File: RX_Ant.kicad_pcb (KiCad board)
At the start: 2 copper layers, 100 x 100 mm, 44 parts, among them J1 CONN_COAXIAL, J10 CONN_COAXIAL, J11 CONN_01X06, J12 CONN_01X05, J13 CONN_COAXIAL, J14 CONN_COAXIAL, J15 CONN_COAXIAL, J16 CONN_01X01, J17 CONN_01X01, J18 CONN_01X01, J19 CONN_01X01, J2 CONN_COAXIAL, J20 CONN_01X01, J21 CONN_01X01, J22 CONN_01X01, J23 CONN_01X01, J3 CONN_COAXIAL, J4 CONN_COAXIAL, J5 CONN_COAXIAL, J6 CONN_COAXIAL, J7 CONN_COAXIAL, J8 CONN_COAXIAL, J9 CONN_COAXIAL

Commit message: RTM 1
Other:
- board text added: "+12 In"
- board text added: "+12V_In"
- board text added: "Alex RX In Board"
- board text added: "Alex TX Out Board"
- board text added: "Ant_1"
- board text added: "Ant_2"
- board text added: "Ant_3"
- board text added: "BYPASS"
- board text added: "EXT1"
- board text added: "EXT2"
- board text added: "From HPF Out"
- board text added: "Gnd"
- board text added: "RX2 IN"
- board text added: "RX2_In"
- board text added: "RX3_In"
- board text added: "RX_Bypass_Out"
- board text added: "To HPF In"
- board text added: "To_RX 1"
- board text added: "To_RX 2"
- board text added: "XVTR RX"
- board text added: "Xvtr_In"

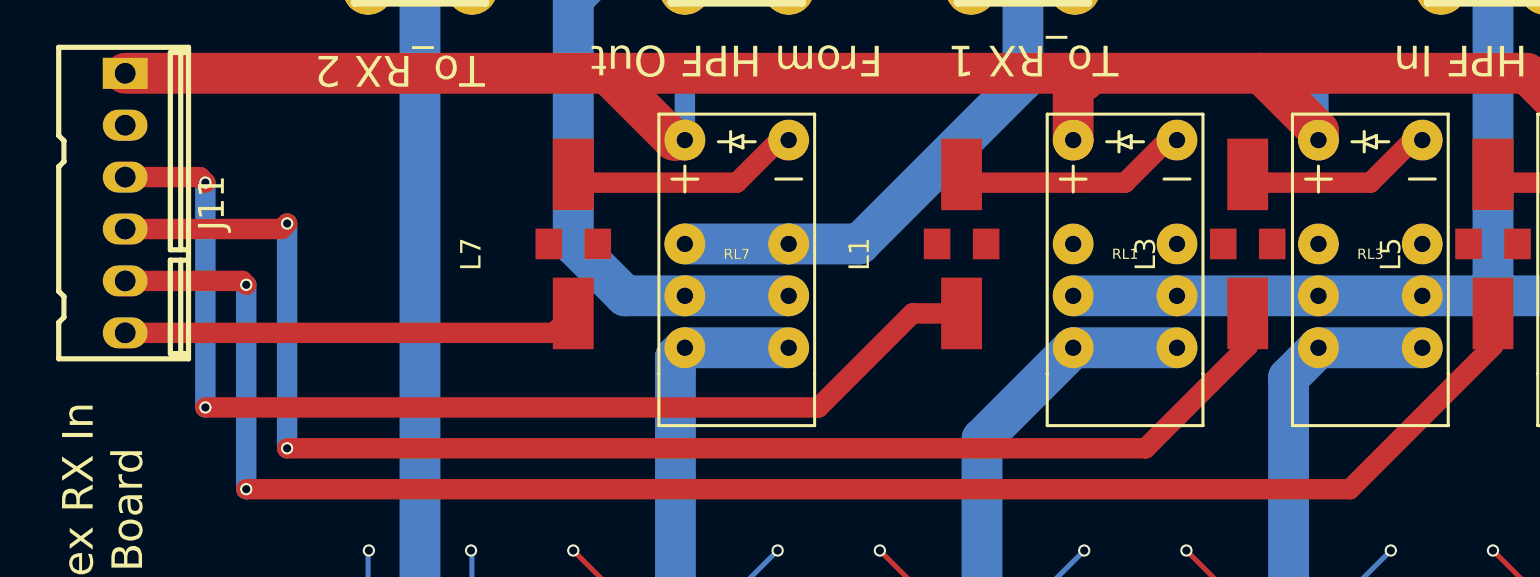
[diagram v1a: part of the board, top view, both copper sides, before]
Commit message: silk and gnd error fixed
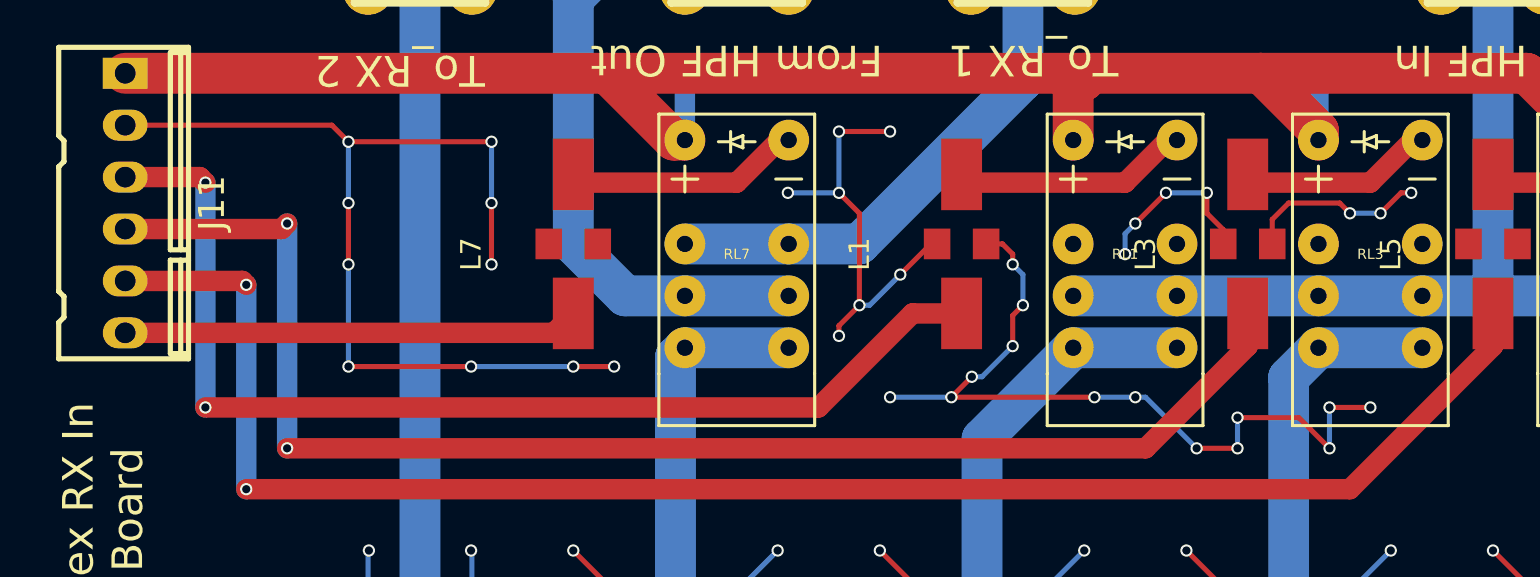
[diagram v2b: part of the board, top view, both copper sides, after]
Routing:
- net GND: track 521.0 -> 646.8 mm, vias 92 -> 130
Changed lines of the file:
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@@
   (general
     (links 136)
-    (no_connects 3)
-    (area 19.899999 23.7808 132.214286 142.700001)
+    (no_connects 2)
+    (area 19.924999 24.924999 120.075001 125.075001)
     (thickness 1.6)
     (drawings 35)
-    (tracks 378)
+    (tracks 473)
     (zones 0)
     (modules 44)
@@
   (gr_line (start 25 25) (end 120 25) (angle 90) (layer Edge.Cuts) (width 0.15))
   (segment (start 61.25 40) (end 61.25 40.55) (width 1) (layer B.Cu) (net 0))
+  (segment (start 44 90) (end 51 90) (width 0.25) (layer F.Cu) (net 1))
+  (via (at 51 96) (size 0.6) (drill 0.4) (layers F.Cu B.Cu) (net 1))
+  (segment (start 51 93) (end 51 96) (width 0.25) (layer F.Cu) (net 1))
+  (via (at 51 93) (size 0.6) (drill 0.4) (layers F.Cu B.Cu) (net 1))
+  (segment (start 51 90) (end 51 93) (width 0.25) (layer B.Cu) (net 1))
+  (via (at 51 90) (size 0.6) (drill 0.4) (layers F.Cu B.Cu) (net 1))
+  (segment (start 68 92.5) (end 65.5 92.5) (width 0.25) (layer B.Cu) (net 1))
+  (via (at 65.5 92.5) (size 0.6) (drill 0.4) (layers F.Cu B.Cu) (net 1))
+  (segment (start 69 98) (end 69 93.5) (width 0.25) (layer F.Cu) (net 1))
+  (via (at 70.5 89.5) (size 0.6) (drill 0.4) (layers F.Cu B.Cu) (net 1))
+  (segment (start 68 89.5) (end 70.5 89.5) (width 0.25) (layer F.Cu) (net 1))
+  (via (at 68 89.5) (size 0.6) (drill 0.4) (layers F.Cu B.Cu) (net 1))
+  (segment (start 68 92.5) (end 68 89.5) (width 0.25) (layer B.Cu) (net 1))
+  (via (at 68 92.5) (size 0.6) (drill 0.4) (layers F.Cu B.Cu) (net 1))
+  (segment (start 69 93.5) (end 68 92.5) (width 0.25) (layer F.Cu) (net 1))
+  (segment (start 87.5 103.5) (end 90.5 103.5) (width 0.25) (layer F.Cu) (net 1))
+  (segment (start 83 102.5) (end 85.5 105) (width 0.25) (layer B.Cu) (net 1))
+  (via (at 85.5 105) (size 0.6) (drill 0.4) (layers F.Cu B.Cu) (net 1))
+  (segment (start 85.5 105) (end 87.5 105) (width 0.25) (layer F.Cu) (net 1))
+  (via (at 87.5 105) (size 0.6) (drill 0.4) (layers F.Cu B.Cu) (net 1))
+  (segment (start 87.5 105) (end 87.5 103.5) (width 0.25) (layer B.Cu) (net 1))
+  (via (at 87.5 103.5) (size 0.6) (drill 0.4) (layers F.Cu B.Cu) (net 1))
+  (segment (start 73.5 102.5) (end 80.5 102.5) (width 0.25) (layer F.Cu) (net 1))
+  (via (at 82.5 102.5) (size 0.6) (drill 0.4) (layers F.Cu B.Cu) (net 1))
+  (segment (start 80.5 102.5) (end 82.5 102.5) (width 0.25) (layer B.Cu) (net 1))
+  (via (at 80.5 102.5) (size 0.6) (drill 0.4) (layers F.Cu B.Cu) (net 1))
+  (segment (start 82.5 102.5) (end 83 102.5) (width 0.25) (layer B.Cu) (net 1))
+  (via (at 94 103) (size 0.6) (drill 0.4) (layers F.Cu B.Cu) (net 1))
+  (segment (start 92 103) (end 94 103) (width 0.25) (layer F.Cu) (net 1))
+  (via (at 92 103) (size 0.6) (drill 0.4) (layers F.Cu B.Cu) (net 1))
+  (segment (start 92 105) (end 92 103) (width 0.25) (layer B.Cu) (net 1))
+  (via (at 92 105) (size 0.6) (drill 0.4) (layers F.Cu B.Cu) (net 1))
+  (segment (start 90.5 103.5) (end 92 105) (width 0.25) (layer F.Cu) (net 1))
+  (segment (start 89.2 95) (end 89.2 93.8) (width 0.25) (layer F.Cu) (net 1) (status 400000))
+  (via (at 96 92.5) (size 0.6) (drill 0.4) (layers F.Cu B.Cu) (net 1))
+  (segment (start 95.5 92.5) (end 96 92.5) (width 0.25) (layer F.Cu) (net 1))
+  (segment (start 94.5 93.5) (end 95.5 92.5) (width 0.25) (layer F.Cu) (net 1))
+  (via (at 94.5 93.5) (size 0.6) (drill 0.4) (layers F.Cu B.Cu) (net 1))
+  (segment (start 93 93.5) (end 94.5 93.5) (width 0.25) (layer B.Cu) (net 1))
+  (via (at 93 93.5) (size 0.6) (drill 0.4) (layers F.Cu B.Cu) (net 1))
+  (segment (start 92.5 93) (end 93 93.5) (width 0.25) (layer F.Cu) (net 1))
+  (segment (start 90 93) (end 92.5 93) (width 0.25) (layer F.Cu) (net 1))
+  (segment (start 89.2 93.8) (end 90 93) (width 0.25) (layer F.Cu) (net 1))
+  (segment (start 86.8 95) (end 86.8 94.3) (width 0.25) (layer F.Cu) (net 1) (status C00000))
+  (segment (start 86.8 94.3) (end 86 93.5) (width 0.25) (layer F.Cu) (net 1) (status 400000))
+  (segment (start 86 93.5) (end 86 92.5) (width 0.25) (layer F.Cu) (net 1))
+  (via (at 86 92.5) (size 0.6) (drill 0.4) (layers F.Cu B.Cu) (net 1))
+  (segment (start 86 92.5) (end 84 92.5) (width 0.25) (layer B.Cu) (net 1))
+  (via (at 84 92.5) (size 0.6) (drill 0.4) (layers F.Cu B.Cu) (net 1))
+  (segment (start 84 92.5) (end 82.5 94) (width 0.25) (layer F.Cu) (net 1))
+  (via (at 82.5 94) (size 0.6) (drill 0.4) (layers F.Cu B.Cu) (net 1))
+  (segment (start 82.5 94) (end 82 94.5) (width 0.25) (layer B.Cu) (net 1))
+  (segment (start 82 94.5) (end 82 95.5) (width 0.25) (layer B.Cu) (net 1))
+  (via (at 82 95.5) (size 0.6) (drill 0.4) (layers F.Cu B.Cu) (net 1))
+  (segment (start 72.8 95) (end 72.5 95) (width 0.25) (layer F.Cu) (net 1))
+  (segment (start 72.5 95) (end 71 96.5) (width 0.25) (layer F.Cu) (net 1))
+  (via (at 71 96.5) (size 0.6) (drill 0.4) (layers F.Cu B.Cu) (net 1))
+  (segment (start 71 96.5) (end 69.5 98) (width 0.25) (layer B.Cu) (net 1))
+  (segment (start 69.5 98) (end 69 98) (width 0.25) (layer B.Cu) (net 1))
+  (via (at 69 98) (size 0.6) (drill 0.4) (layers F.Cu B.Cu) (net 1))
+  (segment (start 69 98) (end 68 99) (width 0.25) (layer F.Cu) (net 1))
+  (segment (start 68 99) (end 68 99.5) (width 0.25) (layer F.Cu) (net 1))
+  (via (at 68 99.5) (size 0.6) (drill 0.4) (layers F.Cu B.Cu) (net 1))
+  (segment (start 75.2 95) (end 76 95) (width 0.25) (layer F.Cu) (net 1))
+  (via (at 70.5 102.5) (size 0.6) (drill 0.4) (layers F.Cu B.Cu) (net 1))
+  (segment (start 73.5 102.5) (end 70.5 102.5) (width 0.25) (layer B.Cu) (net 1))
+  (via (at 73.5 102.5) (size 0.6) (drill 0.4) (layers F.Cu B.Cu) (net 1))
+  (segment (start 74.5 101.5) (end 73.5 102.5) (width 0.25) (layer F.Cu) (net 1))
+  (via (at 74.5 101.5) (size 0.6) (drill 0.4) (layers F.Cu B.Cu) (net 1))
+  (segment (start 75 101.5) (end 74.5 101.5) (width 0.25) (layer B.Cu) (net 1))
+  (segment (start 76.5 100) (end 75 101.5) (width 0.25) (layer B.Cu) (net 1))
+  (via (at 76.5 100) (size 0.6) (drill 0.4) (layers F.Cu B.Cu) (net 1))
+  (segment (start 76.5 98.5) (end 76.5 100) (width 0.25) (layer F.Cu) (net 1))
+  (segment (start 77 98) (end 76.5 98.5) (width 0.25) (layer F.Cu) (net 1))
+  (via (at 77 98) (size 0.6) (drill 0.4) (layers F.Cu B.Cu) (net 1))
+  (segment (start 77 96.5) (end 77 98) (width 0.25) (layer B.Cu) (net 1))
+  (segment (start 76.5 96) (end 77 96.5) (width 0.25) (layer B.Cu) (net 1))
+  (via (at 76.5 96) (size 0.6) (drill 0.4) (layers F.Cu B.Cu) (net 1))
+  (segment (start 76.5 95.5) (end 76.5 96) (width 0.25) (layer F.Cu) (net 1))
+  (segment (start 76 95) (end 76.5 95.5) (width 0.25) (layer F.Cu) (net 1))
+  (segment (start 33.0762 89.19) (end 43.19 89.19) (width 0.25) (layer F.Cu) (net 1))
+  (via (at 57 101) (size 0.6) (drill 0.4) (layers F.Cu B.Cu) (net 1))
+  (segment (start 55 101) (end 57 101) (width 0.25) (layer F.Cu) (net 1))
+  (via (at 55 101) (size 0.6) (drill 0.4) (layers F.Cu B.Cu) (net 1))
+  (segment (start 50 101) (end 55 101) (width 0.25) (layer B.Cu) (net 1))
+  (via (at 50 101) (size 0.6) (drill 0.4) (layers F.Cu B.Cu) (net 1))
+  (segment (start 44 101) (end 50 101) (width 0.25) (layer F.Cu) (net 1))
+  (via (at 44 101) (size 0.6) (drill 0.4) (layers F.Cu B.Cu) (net 1))
+  (segment (start 44 96) (end 44 101) (width 0.25) (layer B.Cu) (net 1))
+  (via (at 44 96) (size 0.6) (drill 0.4) (layers F.Cu B.Cu) (net 1))
+  (segment (start 44 93) (end 44 96) (width 0.25) (layer F.Cu) (net 1))
+  (via (at 44 93) (size 0.6) (drill 0.4) (layers F.Cu B.Cu) (net 1))
+  (segment (start 44 90) (end 44 93) (width 0.25) (layer B.Cu) (net 1))
+  (via (at 44 90) (size 0.6) (drill 0.4) (layers F.Cu B.Cu) (net 1))
+  (segment (start 43.19 89.19) (end 44 90) (width 0.25) (layer F.Cu) (net 1))
   (segment (start 115 30) (end 115 35) (width 0.25) (layer F.Cu) (net 1))
   (via (at 115 65) (size 0.6) (drill 0.4) (layers F.Cu B.Cu) (net 1))

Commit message: Readme cleaning, add 2 3D pictures
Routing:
- net GND: track 646.8 -> 661.1 mm, vias 130 -> 137
- net (no net): track 0.55 -> 0.00 mm
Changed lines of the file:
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@@
   (general
     (links 136)
-    (no_connects 2)
+    (no_connects 1)
     (area 19.924999 24.924999 120.075001 125.075001)
     (thickness 1.6)
     (drawings 35)
-    (tracks 473)
+    (tracks 494)
     (zones 0)
     (modules 44)
@@
       (net 1 GND))
   )
-  (gr_text Ant_3 (at 36 48) (layer B.SilkS)
+  (gr_text Ant_3 (at 34.5 47.75) (layer B.SilkS)
     (effects (font (size 1.5 1.5) (thickness 0.3)) (justify right mirror))
   )
-  (gr_text Ant_2 (at 36 45) (layer B.SilkS)
+  (gr_text Ant_2 (at 34.5 44.75) (layer B.SilkS)
     (effects (font (size 1.5 1.5) (thickness 0.3)) (justify right mirror))
   )
-  (gr_text Ant_1 (at 36 42) (layer B.SilkS)
+  (gr_text Ant_1 (at 34.5 42) (layer B.SilkS)
     (effects (font (size 1.5 1.5) (thickness 0.3)) (justify right mirror))
   )
-  (gr_text "Gnd\n" (at 36 40) (layer B.SilkS)
+  (gr_text "Gnd\n" (at 34.25 40) (layer B.SilkS)
     (effects (font (size 1.5 1.5) (thickness 0.3)) (justify right mirror))
   )
-  (gr_text +12V_In (at 36 37) (layer B.SilkS)
+  (gr_text +12V_In (at 34.25 37) (layer B.SilkS)
     (effects (font (size 1.5 1.5) (thickness 0.3)) (justify right mirror))
   )
-  (gr_text RX_Bypass_Out (at 38 100) (layer B.SilkS)
+  (gr_text RX_Bypass_Out (at 35 99.75) (layer B.SilkS)
     (effects (font (size 1.5 1.5) (thickness 0.3)) (justify right mirror))
   )
-  (gr_text RX3_In (at 38 97) (layer B.SilkS)
+  (gr_text RX3_In (at 35 97) (layer B.SilkS)
     (effects (font (size 1.5 1.5) (thickness 0.3)) (justify right mirror))
   )
-  (gr_text "RX2_In\n" (at 38 94) (layer B.SilkS)
+  (gr_text "RX2_In\n" (at 35 94) (layer B.SilkS)
     (effects (font (size 1.5 1.5) (thickness 0.3)) (justify right mirror))
   )
-  (gr_text Xvtr_In (at 38 91) (layer B.SilkS)
+  (gr_text Xvtr_In (at 35 91) (layer B.SilkS)
     (effects (font (size 1.5 1.5) (thickness 0.3)) (justify right mirror))
   )
-  (gr_text Gnd (at 38 89) (layer B.SilkS)
+  (gr_text Gnd (at 35 89) (layer B.SilkS)
     (effects (font (size 1.5 1.5) (thickness 0.3)) (justify right mirror))
   )
-  (gr_text "+12 In" (at 38 86) (layer B.SilkS)
+  (gr_text "+12 In" (at 35 86.75) (layer B.SilkS)
     (effects (font (size 1.5 1.5) (thickness 0.3)) (justify right mirror))
   )
@@
   (gr_line (start 20 75) (end 25 75) (angle 90) (layer Eco2.User) (width 0.2))
   (gr_line (start 120 75) (end 110 75) (angle 90) (layer Eco2.User) (width 0.2))
-  (gr_text "To PS/SWR Brd" (at 71 36) (layer F.SilkS)
+  (gr_text "To PS/SWR Brd" (at 71 36 180) (layer F.SilkS)
     (effects (font (size 2 2) (thickness 0.3)))
   )
@@
   (gr_line (start 120 25) (end 120 75) (angle 90) (layer Edge.Cuts) (width 0.15))
   (gr_line (start 25 25) (end 120 25) (angle 90) (layer Edge.Cuts) (width 0.15))
-  (segment (start 61.25 40) (end 61.25 40.55) (width 1) (layer B.Cu) (net 0))
+  (segment (start 105.75 95.25) (end 105.75 94.75) (width 0.25) (layer F.Cu) (net 1))
+  (segment (start 101.2 93.8) (end 101.75 93.25) (width 0.25) (layer F.Cu) (net 1))
+  (segment (start 101.75 93.25) (end 105 93.25) (width 0.25) (layer F.Cu) (net 1))
+  (segment (start 105 93.25) (end 105.5 93.75) (width 0.25) (layer F.Cu) (net 1))
+  (via (at 105.5 93.75) (size 0.6) (drill 0.4) (layers F.Cu B.Cu) (net 1))
+  (segment (start 105.5 93.75) (end 105.75 94) (width 0.25) (layer B.Cu) (net 1))
+  (segment (start 105.75 94) (end 105.75 95.25) (width 0.25) (layer B.Cu) (net 1))
+  (via (at 105.75 95.25) (size 0.6) (drill 0.4) (layers F.Cu B.Cu) (net 1))
+  (segment (start 101.2 95) (end 101.2 93.8) (width 0.25) (layer F.Cu) (net 1) (status 400000))
+  (via (at 108.5 92.5) (size 0.6) (drill 0.4) (layers F.Cu B.Cu) (net 1))
+  (segment (start 108 92.5) (end 108.5 92.5) (width 0.25) (layer B.Cu) (net 1))
+  (segment (start 106.75 93.75) (end 108 92.5) (width 0.25) (layer B.Cu) (net 1))
+  (via (at 106.75 93.75) (size 0.6) (drill 0.4) (layers F.Cu B.Cu) (net 1))
+  (segment (start 105.75 94.75) (end 106.75 93.75) (width 0.25) (layer F.Cu) (net 1))
+  (segment (start 98.8 95) (end 98.8 94.05) (width 0.25) (layer F.Cu) (net 1) (status 400000))
+  (via (at 97.75 92.5) (size 0.6) (drill 0.4) (layers F.Cu B.Cu) (net 1))
+  (segment (start 97.75 93) (end 97.75 92.5) (width 0.25) (layer F.Cu) (net 1))
+  (segment (start 98.8 94.05) (end 97.75 93) (width 0.25) (layer F.Cu) (net 1))
+  (via (at 89.2 95) (size 0.6) (drill 0.4) (layers F.Cu B.Cu) (net 1) (status C00000))
+  (segment (start 89.5 93.75) (end 90 93.25) (width 0.25) (layer F.Cu) (net 1))
+  (segment (start 90 93.25) (end 92.5 93.25) (width 0.25) (layer F.Cu) (net 1))
+  (segment (start 92.5 93.25) (end 93 93.5) (width 0.25) (layer F.Cu) (net 1))
+  (via (at 93 93.5) (size 0.6) (drill 0.4) (layers F.Cu B.Cu) (net 1))
+  (segment (start 93 93.5) (end 94.5 93.5) (width 0.25) (layer B.Cu) (net 1))
+  (via (at 94.5 93.5) (size 0.6) (drill 0.4) (layers F.Cu B.Cu) (net 1))
+  (segment (start 94.5 93.5) (end 95.5 92.5) (width 0.25) (layer F.Cu) (net 1))
+  (segment (start 96 92.5) (end 95.5 92.5) (width 0.25) (layer F.Cu) (net 1))
+  (via (at 96 92.5) (size 0.6) (drill 0.4) (layers F.Cu B.Cu) (net 1))
+  (segment (start 89.2 95) (end 89.5 93.75) (width 0.25) (layer F.Cu) (net 1) (status 400000))
+  (segment (start 89.2 95) (end 89.25 95) (width 0.25) (layer B.Cu) (net 1) (status 400000))
+  (via (at 86.75 95) (size 0.6) (drill 0.4) (layers F.Cu B.Cu) (net 1) (status 800000))
+  (segment (start 86.75 95) (end 86.8 95) (width 0.25) (layer F.Cu) (net 1) (status C00000))
   (segment (start 44 90) (end 51 90) (width 0.25) (layer F.Cu) (net 1))
   (via (at 51 96) (size 0.6) (drill 0.4) (layers F.Cu B.Cu) (net 1))
@@
   (via (at 92 105) (size 0.6) (drill 0.4) (layers F.Cu B.Cu) (net 1))
   (segment (start 90.5 103.5) (end 92 105) (width 0.25) (layer F.Cu) (net 1))
-  (segment (start 89.2 95) (end 89.2 93.8) (width 0.25) (layer F.Cu) (net 1) (status 400000))
-  (via (at 96 92.5) (size 0.6) (drill 0.4) (layers F.Cu B.Cu) (net 1))
-  (segment (start 95.5 92.5) (end 96 92.5) (width 0.25) (layer F.Cu) (net 1))
-  (segment (start 94.5 93.5) (end 95.5 92.5) (width 0.25) (layer F.Cu) (net 1))
-  (via (at 94.5 93.5) (size 0.6) (drill 0.4) (layers F.Cu B.Cu) (net 1))
-  (segment (start 93 93.5) (end 94.5 93.5) (width 0.25) (layer B.Cu) (net 1))
-  (via (at 93 93.5) (size 0.6) (drill 0.4) (layers F.Cu B.Cu) (net 1))
-  (segment (start 92.5 93) (end 93 93.5) (width 0.25) (layer F.Cu) (net 1))
-  (segment (start 90 93) (end 92.5 93) (width 0.25) (layer F.Cu) (net 1))
-  (segment (start 89.2 93.8) (end 90 93) (width 0.25) (layer F.Cu) (net 1))
-  (segment (start 86.8 95) (end 86.8 94.3) (width 0.25) (layer F.Cu) (net 1) (status C00000))
-  (segment (start 86.8 94.3) (end 86 93.5) (width 0.25) (layer F.Cu) (net 1) (status 400000))
+  (segment (start 86.8 95) (end 86.8 94.3) (width 0.25) (layer F.Cu) (net 1))
+  (segment (start 86.8 94.3) (end 86 93.5) (width 0.25) (layer F.Cu) (net 1))
   (segment (start 86 93.5) (end 86 92.5) (width 0.25) (layer F.Cu) (net 1))
   (via (at 86 92.5) (size 0.6) (drill 0.4) (layers F.Cu B.Cu) (net 1))
